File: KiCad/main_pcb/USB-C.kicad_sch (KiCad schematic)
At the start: 7 parts, among them J2 USB-C, U10 JSMSEMI AMS1117-3.3V, U8 CH340C

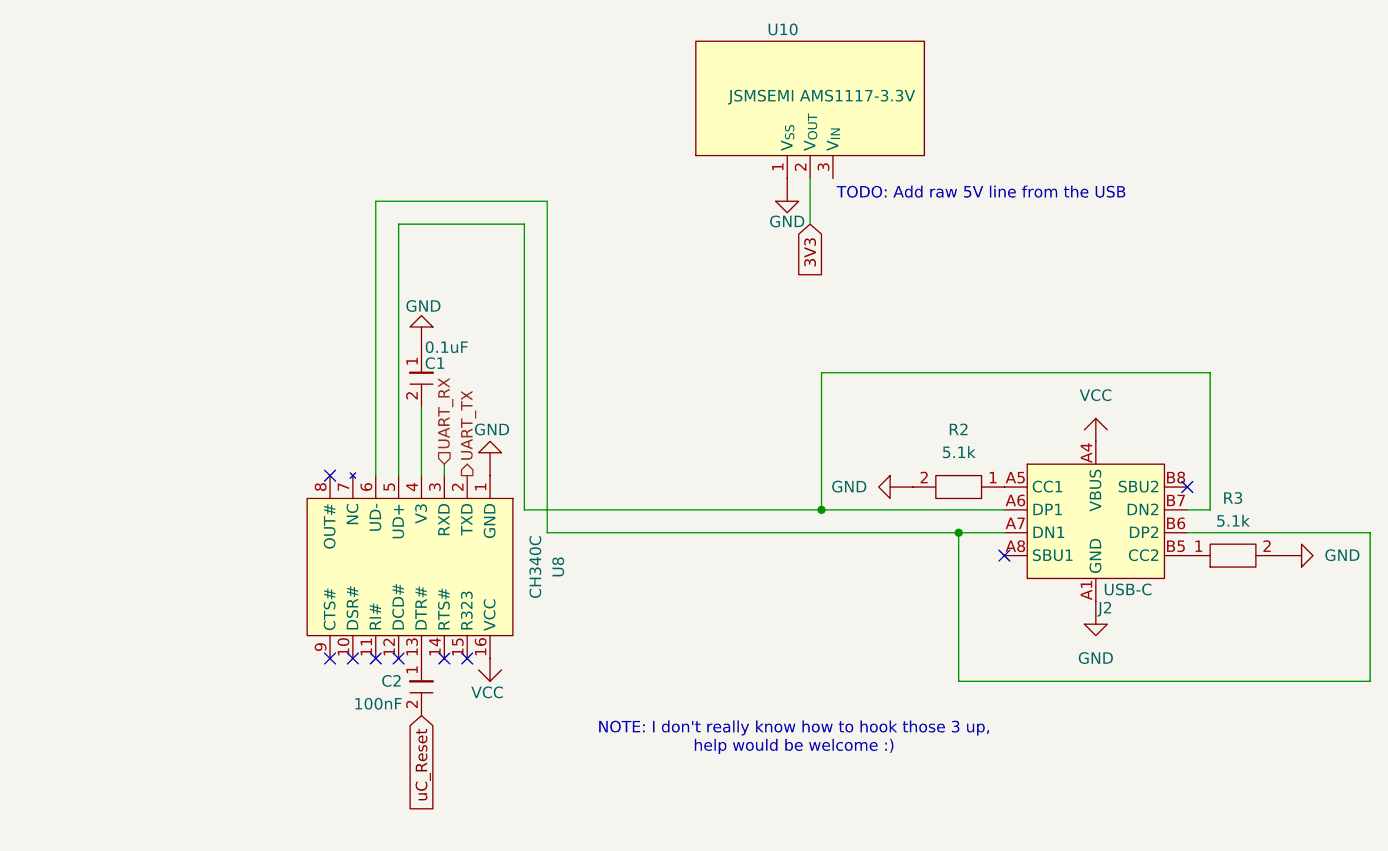
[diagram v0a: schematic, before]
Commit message: feat(KiCad): Continues work on main PCB circuit
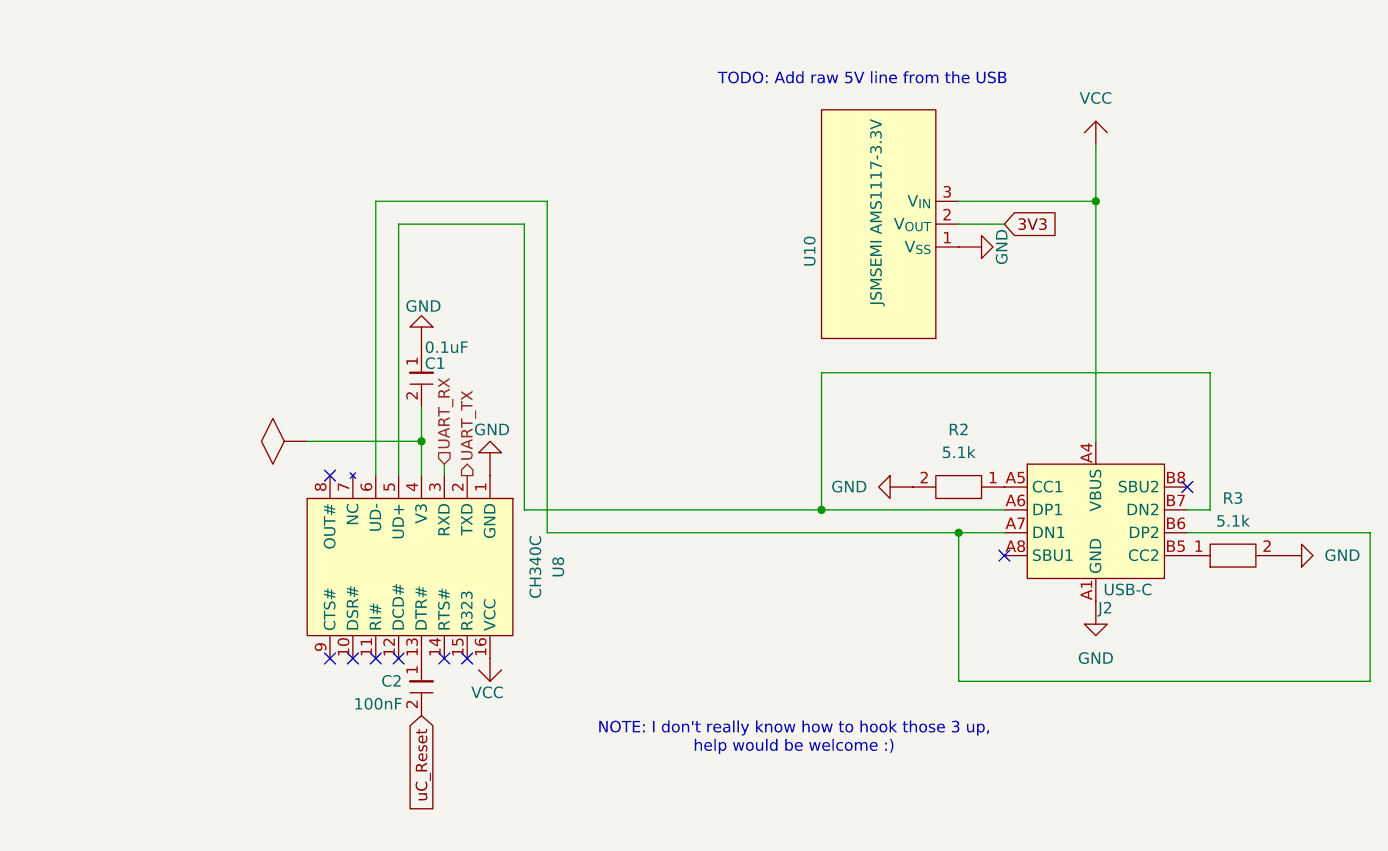
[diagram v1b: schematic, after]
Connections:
- net VBUS: now also U10.3 (V_{IN})
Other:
- moved on the sheet: U10
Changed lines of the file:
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@@
 	(text "TODO: Add raw 5V line from the USB"
 		(exclude_from_sim no)
-		(at 156.21 70.358 0)
+		(at 143.002 57.658 0)
 		(effects
 			(font
@@
 	)
 	(junction
+		(at 93.98 97.79)
+		(diameter 0)
+		(color 0 0 0 0)
+	)
+	(junction
+		(at 168.91 71.12)
+		(diameter 0)
+		(color 0 0 0 0)
+	)
+	(junction
 		(at 138.43 105.41)
 		(diameter 0)
@@
 	(wire
 		(pts
+			(xy 168.91 64.77) (xy 168.91 71.12)
+		)
+		(stroke
+			(width 0)
+			(type default)
+		)
+	)
+	(wire
+		(pts
+			(xy 93.98 97.79) (xy 93.98 101.6)
+		)
+		(stroke
+			(width 0)
+			(type default)
+		)
+	)
+	(wire
+		(pts
 			(xy 153.67 107.95) (xy 158.75 107.95)
 		)
@@
 	(wire
 		(pts
-			(xy 93.98 93.98) (xy 93.98 101.6)
-		)
-		(stroke
-			(width 0)
-			(type default)
-		)
-	)
-	(wire
-		(pts
-			(xy 137.16 73.66) (xy 137.16 68.58)
+			(xy 93.98 93.98) (xy 93.98 97.79)
+		)
+		(stroke
+			(width 0)
+			(type default)
+		)
+	)
+	(wire
+		(pts
+			(xy 81.28 97.79) (xy 93.98 97.79)
+		)
+		(stroke
+			(width 0)
+			(type default)
+		)
+	)
+	(wire
+		(pts
+			(xy 158.75 73.66) (xy 153.67 73.66)
 		)
 		(stroke
@@
 	(wire
 		(pts
+			(xy 168.91 71.12) (xy 168.91 97.79)
+		)
+		(stroke
+			(width 0)
+			(type default)
+		)
+	)
+	(wire
+		(pts
 			(xy 138.43 105.41) (xy 158.75 105.41)
 		)
@@
 		(pts
 			(xy 88.9 71.12) (xy 88.9 101.6)
+		)
+		(stroke
+			(width 0)
+			(type default)
+		)
+	)
+	(wire
+		(pts
+			(xy 153.67 71.12) (xy 168.91 71.12)
 		)
 		(stroke
@@
 	(global_label "3V3"
 		(shape input)
-		(at 137.16 73.66 270)
+		(at 158.75 73.66 0)
 		(fields_autoplaced yes)
 		(effects
@@
 				(size 1.27 1.27)
 			)
-			(justify right)
+			(justify left)
 		)
 		(property "Intersheetrefs" "${INTERSHEET_REFS}"
-			(at 137.16 80.1528 90)
-			(hide yes)
-			(show_name no)
-			(do_not_autoplace no)
-			(effects
-				(font
-					(size 1.27 1.27)
-				)
-				(justify right)
+			(at 165.2428 73.66 0)
+			(hide yes)
+			(show_name no)
+			(do_not_autoplace no)
+			(effects
+				(font
+					(size 1.27 1.27)
+				)
+				(justify left)
 			)
 		)
@@
 	)
 	(symbol
-		(lib_id "Lily's_Pad:VCC")
-		(at 168.91 95.25 180)
-		(unit 1)
-		(body_style 1)
-		(exclude_from_sim no)
-		(in_bom no)
-		(on_board no)
-		(in_pos_files yes)
-		(dnp no)
-		(fields_autoplaced yes)
-		(property "Reference" "#PWR021"
-			(at 168.91 93.98 0)
-			(hide yes)
-			(show_name no)
-			(do_not_autoplace no)
-			(effects
-				(font
-					(size 1.27 1.27)
-				)
-			)
-		)
-		(property "Value" "VCC"
-			(at 168.91 92.71 0)
-			(show_name no)
-			(do_not_autoplace no)
-			(effects
-				(font
-					(size 1.27 1.27)
-				)
-			)
-		)
-		(property "Footprint" ""
-			(at 168.91 95.25 0)
-			(hide yes)
-			(show_name no)
-			(do_not_autoplace no)
-			(effects
-				(font
-					(size 1.27 1.27)
-				)
-			)
-		)
-		(property "Datasheet" ""
-			(at 168.91 95.25 0)
-			(hide yes)
-			(show_name no)
-			(do_not_autoplace no)
-			(effects
-				(font
-					(size 1.27 1.27)
-				)
-			)
-		)
-		(property "Description" ""
-			(at 168.91 95.25 0)
-			(hide yes)
-			(show_name no)
-			(do_not_autoplace no)
-			(effects
-				(font
-					(size 1.27 1.27)
-				)
-			)
-		)
-		(pin "1"
-		)
-		(instances
-			(project "main_pcb"
-				(path "/346fb29b-2426-4b69-9f9a-e979b6e41832/a4816677-4d4e-4f2e-882a-ab61f6eb2b02"
-					(reference "#PWR021")
-					(unit 1)
-				)
-			)
-		)
-	)
-	(symbol
 		(lib_id "Lily's_Pad:GND")
 		(at 93.98 85.09 180)
@@
 				(path "/346fb29b-2426-4b69-9f9a-e979b6e41832/a4816677-4d4e-4f2e-882a-ab61f6eb2b02"
 					(reference "#PWR012")
+					(unit 1)
+				)
+			)
+		)
+	)
+	(symbol
+		(lib_id "Lily's_Pad:VCC")
+		(at 168.91 62.23 180)
+		(unit 1)
+		(body_style 1)
+		(exclude_from_sim no)
+		(in_bom no)
+		(on_board no)
+		(in_pos_files yes)
+		(dnp no)
+		(fields_autoplaced yes)
+		(property "Reference" "#PWR021"
+			(at 168.91 60.96 0)
+			(hide yes)
+			(show_name no)
+			(do_not_autoplace no)
+			(effects
+				(font
+					(size 1.27 1.27)
+				)
+			)
+		)
+		(property "Value" "VCC"
+			(at 168.91 59.69 0)
+			(show_name no)
+			(do_not_autoplace no)
+			(effects
+				(font
+					(size 1.27 1.27)
+				)
+			)
+		)
+		(property "Footprint" ""
+			(at 168.91 62.23 0)
+			(hide yes)
+			(show_name no)
+			(do_not_autoplace no)
+			(effects
+				(font
+					(size 1.27 1.27)
+				)
+			)
+		)
+		(property "Datasheet" ""
+			(at 168.91 62.23 0)
+			(hide yes)
+			(show_name no)
+			(do_not_autoplace no)
+			(effects
+				(font
+					(size 1.27 1.27)
+				)
+			)
+		)
+		(property "Description" ""
+			(at 168.91 62.23 0)
+			(hide yes)
+			(show_name no)
+			(do_not_autoplace no)
+			(effects
+				(font
+					(size 1.27 1.27)
+				)
+			)
+		)
+		(pin "1"
+		)
+		(instances
+			(project "main_pcb"
+				(path "/346fb29b-2426-4b69-9f9a-e979b6e41832/a4816677-4d4e-4f2e-882a-ab61f6eb2b02"
+					(reference "#PWR021")
 					(unit 1)
 				)
@@
 	)
 	(symbol
+		(lib_id "Lily's_Pad:PWR_FLG")
+		(at 78.74 97.79 270)
+		(unit 1)
+		(body_style 1)
+		(exclude_from_sim no)
+		(in_bom no)
+		(on_board no)
+		(in_pos_files yes)
+		(dnp no)
+		(fields_autoplaced yes)
+		(property "Reference" "#PWR027"
+			(at 78.74 97.79 0)
+			(hide yes)
+			(show_name no)
+			(do_not_autoplace no)
+			(effects
+				(font
+					(size 1.27 1.27)
+				)
+			)
+		)
+		(property "Value" "PWR_FLG"
+			(at 78.74 97.79 0)
+			(hide yes)
+			(show_name no)
+			(do_not_autoplace no)
+			(effects
+				(font
+					(size 1.27 1.27)
+				)
+			)
+		)
+		(property "Footprint" ""
+			(at 78.74 97.79 0)
+			(hide yes)
+			(show_name no)
+			(do_not_autoplace no)
+			(effects
+				(font
+					(size 1.27 1.27)
+				)
+			)
+		)
+		(property "Datasheet" ""
+			(at 78.74 97.79 0)
+			(hide yes)
+			(show_name no)
+			(do_not_autoplace no)
+			(effects
+				(font
+					(size 1.27 1.27)
+				)
+			)
+		)
+		(property "Description" ""
+			(at 78.74 97.79 0)
+			(hide yes)
+			(show_name no)
+			(do_not_autoplace no)
+			(effects
+				(font
+					(size 1.27 1.27)
+				)
+			)
+		)
+		(pin "1"
+		)
+		(instances
+			(project "main_pcb"
+				(path "/346fb29b-2426-4b69-9f9a-e979b6e41832/a4816677-4d4e-4f2e-882a-ab61f6eb2b02"
+					(reference "#PWR027")
+					(unit 1)
+				)
+			)
+		)
+	)
+	(symbol
 		(lib_id "Lily's_Pad:JSMSEMI_AMS1117-3.3V")
-		(at 137.16 59.69 90)
+		(at 144.78 73.66 180)
 		(unit 1)
 		(body_style 1)
@@
 		(dnp no)
 		(property "Reference" "U10"
-			(at 135.8899 52.07 90)
+			(at 137.16 74.9301 90)
 			(show_name no)
 			(do_not_autoplace no)
@@
 		)
 		(property "Value" "JSMSEMI AMS1117-3.3V"
-			(at 148.844 59.436 90)
+			(at 144.526 61.976 90)
 			(show_name no)
 			(do_not_autoplace no)
@@
 		)
 		(property "Footprint" ""
-			(at 137.16 59.69 0)
+			(at 144.78 73.66 0)
 			(hide yes)
 			(show_name no)
@@
 		)
 		(property "Datasheet" "file:///Users/apetitco/Documents/Module Elec - Lily's Pad/Datasheets/U - Integrated Circuits/Voltage Regulators/JSMSEMI_AMS1117-3.3V.pdf"
-			(at 137.16 59.69 0)
+			(at 144.78 73.66 0)
 			(hide yes)
 			(show_name no)
@@
 		)
 		(property "Description" ""
-			(at 137.16 59.69 0)
+			(at 144.78 73.66 0)
 			(hide yes)
 			(show_name no)
@@
 	(symbol
 		(lib_id "Lily's_Pad:GND")
-		(at 134.62 71.12 0)
+		(at 156.21 76.2 90)
 		(unit 1)
 		(body_style 1)
@@
 		(dnp no)
 		(property "Reference" "#PWR022"
-			(at 134.62 73.66 0)
+			(at 158.75 76.2 0)
 			(hide yes)
 			(show_name no)
@@
 		)
 		(property "Value" "GND"
-			(at 134.62 73.406 0)
+			(at 158.496 76.2 0)
 			(show_name no)
 			(do_not_autoplace no)
@@
 		)
 		(property "Footprint" ""
-			(at 134.62 71.12 0)
+			(at 156.21 76.2 0)
 			(hide yes)
 			(show_name no)
@@
 		)
 		(property "Datasheet" ""
-			(at 134.62 71.12 0)
+			(at 156.21 76.2 0)
 			(hide yes)
 			(show_name no)
@@
 		)
 		(property "Description" ""
-			(at 134.62 71.12 0)
-			(hide yes)
-			(show_name no)
+			(at 156.21 76.2 0)
+			(hide yes)
+			(show_name no)

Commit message: feat(KiCad): Continues work on main PCB circuit
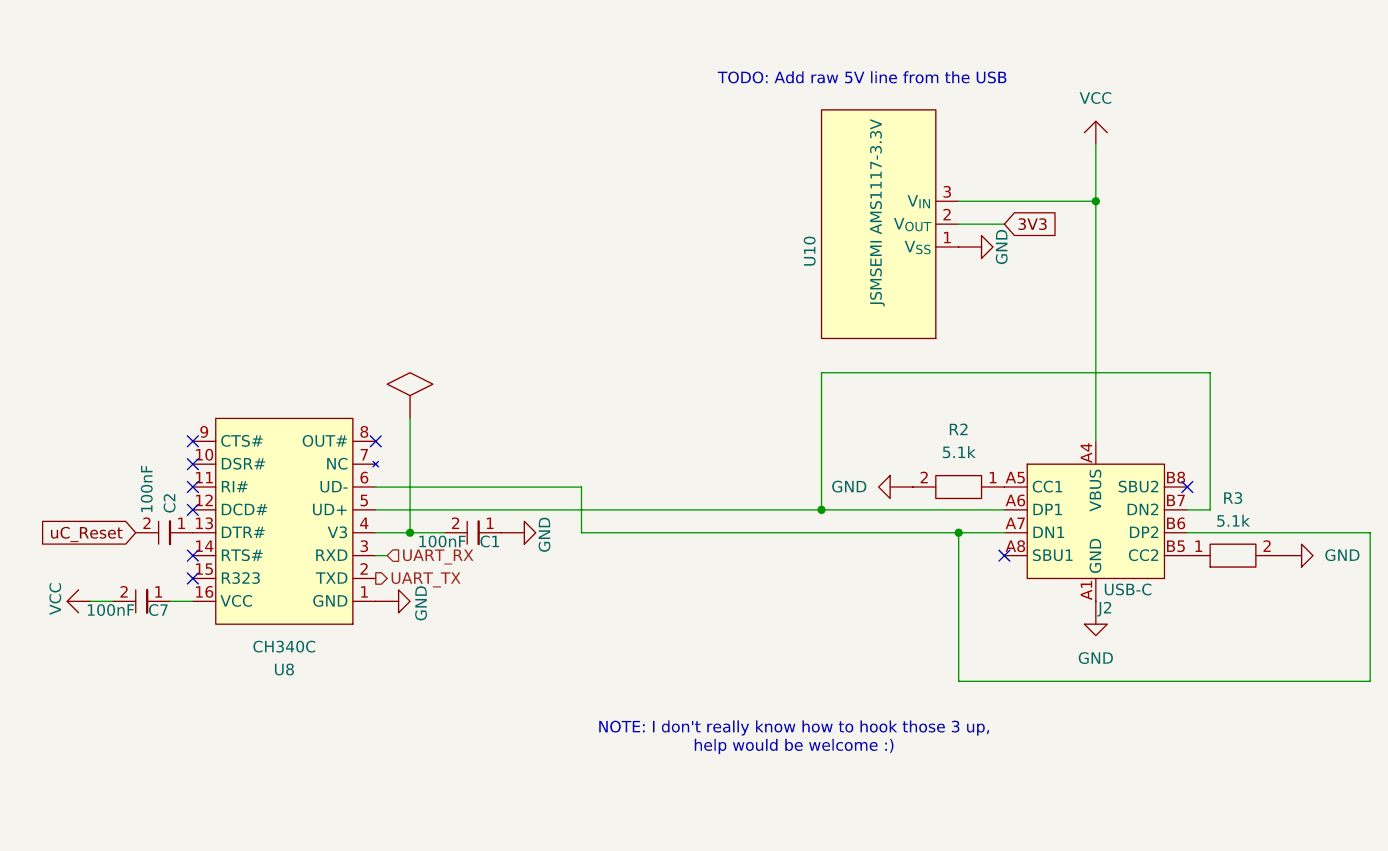
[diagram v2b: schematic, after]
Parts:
- added C7: 100nF, symbol Lily's_Pad:Capacitor
- C1: value 0.1uF -> 100nF
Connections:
- net VBUS: now also C7.2; no longer U8.16 (VCC)
- new net: C7.1, U8.16 (VCC)
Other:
- moved on the sheet: C1, C2, U8

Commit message: feat(KiCad): Continues work on main PCB circuit
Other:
- note added: "TODO: Add raw 5V line from the USB & add capacitors"
- note removed: "TODO: Add raw 5V line from the USB"
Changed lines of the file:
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@@
 	(generator_version "10.0")
 	(paper "A4")
-	(text "TODO: Add raw 5V line from the USB"
+	(text "TODO: Add raw 5V line from the USB\n&\nadd capacitors"
 		(exclude_from_sim no)
 		(at 143.002 57.658 0)

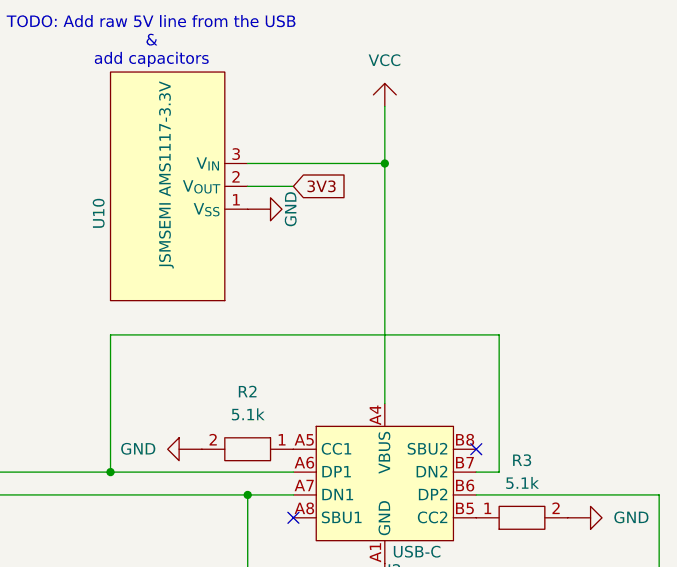
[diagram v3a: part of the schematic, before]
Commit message: feat(KiCad): Continues work on main PCB circuit
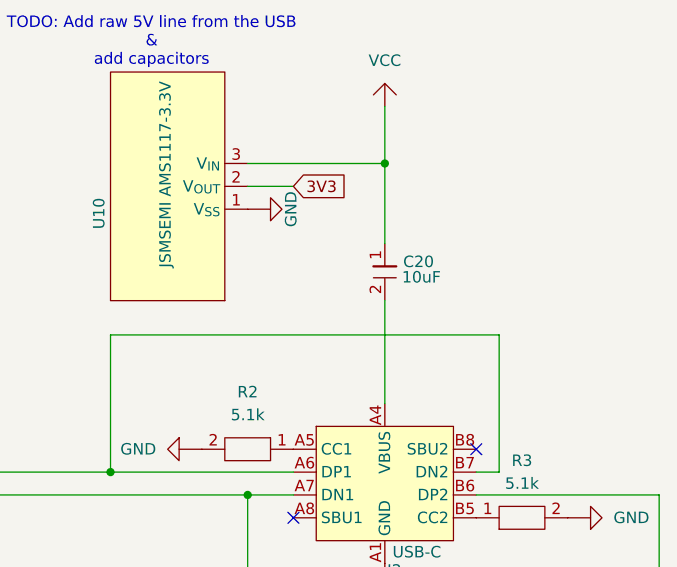
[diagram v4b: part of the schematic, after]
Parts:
- added C20: 10uF, symbol Lily's_Pad:Capacitor
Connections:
- net VBUS: now also C20.2; no longer C7.2, U10.3 (V_{IN})
- new net VCC: C20.1, C7.2, U10.3 (V_{IN})
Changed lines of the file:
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@@
+	(wire
+		(pts
+			(xy 168.91 86.36) (xy 168.91 97.79)
+		)
+		(stroke
+			(width 0)
+			(type default)
+		)
+	)
 	(wire
 		(pts
@@
 	(wire
 		(pts
-			(xy 168.91 71.12) (xy 168.91 97.79)
+			(xy 168.91 71.12) (xy 168.91 80.01)
 		)
 		(stroke
@@
 					(unit 1)
 				)
+			)
+		)
+	)
+	(symbol
+		(lib_id "Lily's_Pad:Capacitor")
+		(at 168.91 83.82 0)
+		(unit 1)
+		(body_style 1)
+		(exclude_from_sim no)
+		(in_bom yes)
+		(on_board yes)
+		(in_pos_files yes)
+		(dnp no)
+		(property "Reference" "C20"
+			(at 170.942 82.042 0)
+			(show_name no)
+			(do_not_autoplace no)
+			(effects
+				(font
+					(size 1.27 1.27)
+				)
+				(justify left)
+			)
+		)
+		(property "Value" "10uF"
+			(at 172.974 83.7566 0)
+			(show_name no)
+			(do_not_autoplace no)
+			(effects
+				(font
+					(size 1.27 1.27)
+				)
+			)
+		)
+		(property "Footprint" ""
+			(at 168.91 83.82 0)
+			(hide yes)
+			(show_name no)
+			(do_not_autoplace no)
+			(effects
+				(font
+					(size 1.27 1.27)
+				)
+			)
+		)
+		(property "Datasheet" ""
+			(at 168.91 83.82 0)
+			(hide yes)
+			(show_name no)
+			(do_not_autoplace no)
+			(effects
+				(font
+					(size 1.27 1.27)
+				)
+			)
+		)
+		(property "Description" ""
+			(at 168.91 83.82 0)
+			(hide yes)
+			(show_name no)
+			(do_not_autoplace no)
+			(effects
+				(font
+					(size 1.27 1.27)
+				)
+			)
+		)
+		(pin "1"
+		)
+		(pin "2"
+		)
+		(instances
+			(project "main_pcb"
+				(path "/346fb29b-2426-4b69-9f9a-e979b6e41832/a4816677-4d4e-4f2e-882a-ab61f6eb2b02"
+					(reference "C20")
+					(unit 1)
+				)

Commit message: feat(KiCad): Continues work on circuit
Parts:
- C1, C2, C20, C7: symbol Lily's_Pad:Capacitor -> lilys_pad:Capacitor
- R2, R3: symbol Lily's_Pad:Resistor -> lilys_pad:Resistor
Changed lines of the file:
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@@
 	)
 	(symbol
-		(lib_id "Lily's_Pad:Capacitor")
+		(lib_id "lilys_pad:Capacitor")
 		(at 168.91 83.82 0)
 		(unit 1)
@@
 	)
 	(symbol
-		(lib_id "Lily's_Pad:Capacitor")
+		(lib_id "lilys_pad:Capacitor")
 		(at 64.77 107.95 270)
 		(unit 1)
@@
 	)
 	(symbol
-		(lib_id "Lily's_Pad:VCC")
+		(lib_id "lilys_pad:VCC")
 		(at 54.61 115.57 270)
 		(unit 1)
@@
 	)
 	(symbol
-		(lib_id "Lily's_Pad:GND")
+		(lib_id "lilys_pad:GND")
 		(at 91.44 115.57 90)
 		(unit 1)
@@
 	)
 	(symbol
-		(lib_id "Lily's_Pad:Resistor")
+		(lib_id "lilys_pad:Resistor")
 		(at 184.15 110.49 90)
 		(unit 1)
@@
 	)
 	(symbol
-		(lib_id "Lily's_Pad:GND")
+		(lib_id "lilys_pad:GND")
 		(at 105.41 107.95 90)
 		(unit 1)
@@
 	)
 	(symbol
-		(lib_id "Lily's_Pad:VCC")
+		(lib_id "lilys_pad:VCC")
 		(at 168.91 62.23 180)
 		(unit 1)
@@
 		)
 		(property "Value" "VCC"
-			(at 168.91 59.69 0)
-			(show_name no)
-			(do_not_autoplace no)
-			(effects
-				(font
-					(size 1.27 1.27)
-				)
+			(at 171.45 62.8649 0)
+			(show_name no)
+			(do_not_autoplace no)
+			(effects
+				(font
+					(size 1.27 1.27)
+				)
+				(justify right)
 			)
 		)
@@
 	)
 	(symbol
-		(lib_id "Lily's_Pad:Capacitor")
+		(lib_id "lilys_pad:Capacitor")
 		(at 99.06 107.95 270)
 		(unit 1)
@@
 	)
 	(symbol
-		(lib_id "Lily's_Pad:Capacitor")
+		(lib_id "lilys_pad:Capacitor")
 		(at 62.23 115.57 270)
 		(unit 1)
@@
 	)
 	(symbol
-		(lib_id "Lily's_Pad:PWR_FLG")
+		(lib_id "lilys_pad:PWR_FLG")
 		(at 92.71 92.71 180)
 		(unit 1)
@@
 	)
 	(symbol
-		(lib_id "Lily's_Pad:GND")
+		(lib_id "lilys_pad:GND")
 		(at 156.21 76.2 90)
 		(unit 1)
@@
 	)
 	(symbol
-		(lib_id "Lily's_Pad:GND")
+		(lib_id "lilys_pad:GND")
 		(at 146.05 102.87 270)
 		(unit 1)
@@
 		)
 		(property "Value" "GND"
-			(at 143.51 102.8699 90)
-			(show_name no)
-			(do_not_autoplace no)
-			(effects
-				(font
-					(size 1.27 1.27)
-				)
-				(justify right)
+			(at 145.415 99.06 90)
+			(show_name no)
+			(do_not_autoplace no)
+			(effects
+				(font
+					(size 1.27 1.27)
+				)
 			)
 		)
@@
 	)
 	(symbol
-		(lib_id "Lily's_Pad:GND")
+		(lib_id "lilys_pad:GND")
 		(at 168.91 118.11 0)
 		(unit 1)
@@
 		)
 		(property "Value" "GND"
-			(at 168.91 121.92 0)
-			(show_name no)
-			(do_not_autoplace no)
-			(effects
-				(font
-					(size 1.27 1.27)
-				)
+			(at 171.45 118.7449 0)
+			(show_name no)
+			(do_not_autoplace no)
+			(effects
+				(font
+					(size 1.27 1.27)
+				)
+				(justify left)
 			)
 		)
@@
 	)
 	(symbol
-		(lib_id "Lily's_Pad:GND")
+		(lib_id "lilys_pad:GND")
 		(at 191.77 110.49 90)
 		(unit 1)
@@
 	)
 	(symbol
-		(lib_id "Lily's_Pad:Resistor")
+		(lib_id "lilys_pad:Resistor")
 		(at 153.67 102.87 270)
 		(unit 1)
